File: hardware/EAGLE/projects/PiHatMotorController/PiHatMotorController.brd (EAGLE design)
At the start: 100 x 80 mm, 86 parts, among them IC2_0_PC JP, U0-C1 0.1uF, U0-C2 1nF, U0-C3 0.22uF, U0-C4 0.1uF, U0-C5 0.22uF, U0-R1 4.7k, U0-R2 47k, U0-R3 10k, U0-R4 10k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

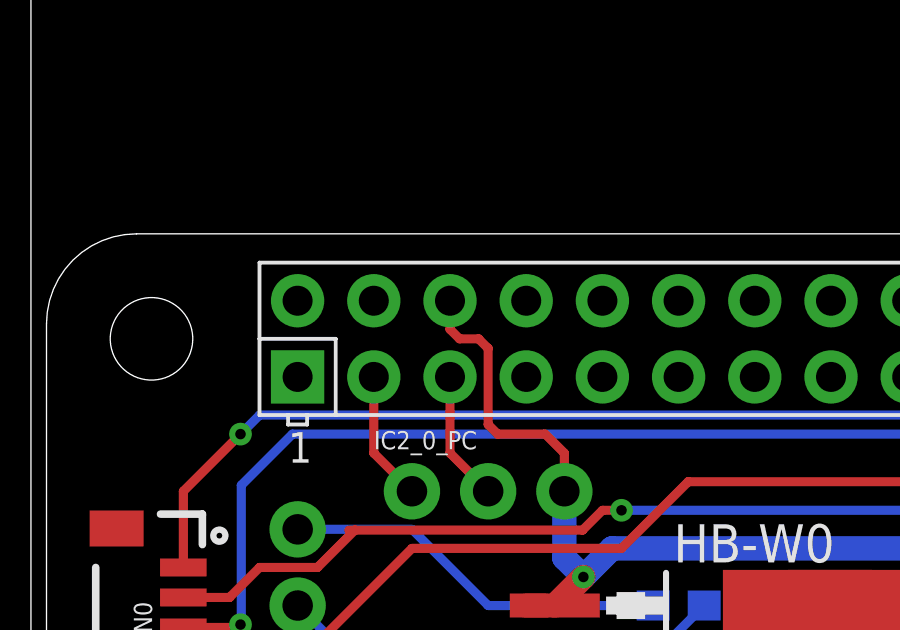
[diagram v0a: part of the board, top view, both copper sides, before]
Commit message: teensy32 board added
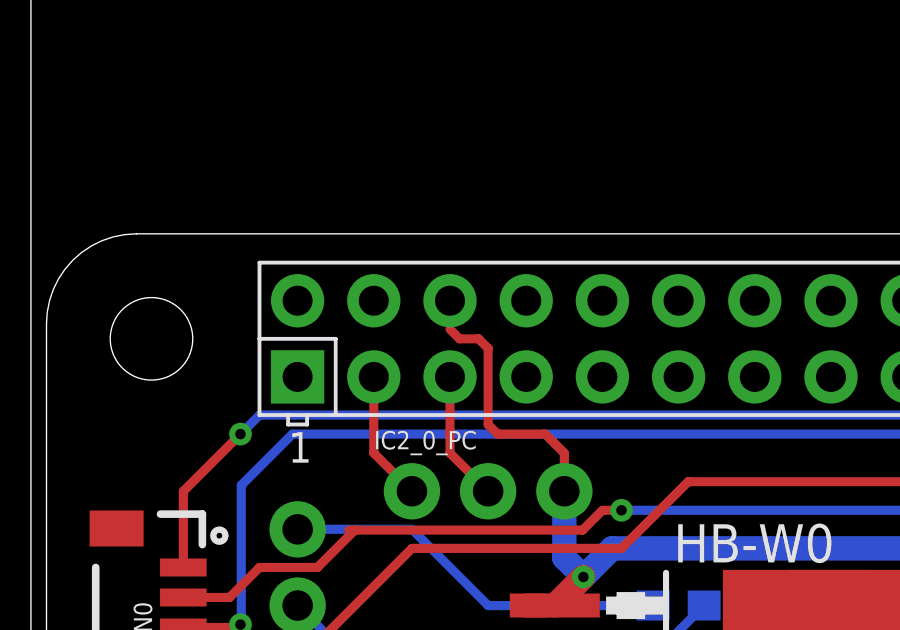
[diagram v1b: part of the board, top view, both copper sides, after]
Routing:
- net GND: track 401.0 -> 400.1 mm
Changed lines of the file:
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@@
 </signal>
 <signal name="GND">
-<contactref element="X1" pad="6"/>
 <contactref element="HB-W0" pad="1" route="any" routetag="G$1.GND"/>
 <contactref element="W0-C3" pad="1"/>
@@
 <wire x1="15.24" y1="53.0225" x2="14.9225" y2="53.34" width="0.3048" layer="1"/>
 <wire x1="14.9225" y1="53.34" x2="14.2875" y2="53.34" width="0.3048" layer="1"/>
-<wire x1="13.968159375" y1="53.659340625" x2="13.968159375" y2="54.61074375" width="0.3048" layer="1"/>
 <wire x1="14.2875" y1="53.34" x2="13.968159375" y2="53.659340625" width="0.3048" layer="1"/>
 <contactref element="BATTERY" pad="3"/>
@@
 <wire x1="57.785" y1="9.525" x2="57.15" y2="8.89" width="0.8128" layer="16"/>
 <wire x1="57.15" y1="8.89" x2="57.15" y2="5.08" width="0.8128" layer="16"/>
+<contactref element="X1" pad="6"/>
 <wire x1="39.155" y1="36.83" x2="39.155" y2="39.37" width="0" layer="19" extent="16-16"/>
 <wire x1="17.145" y1="44.45" x2="17.4625" y2="44.45" width="0" layer="19" extent="1-1"/>
+<wire x1="13.968159375" y1="54.61074375" x2="13.968159375" y2="53.659340625" width="0" layer="19" extent="1-1"/>
 <wire x1="34.71" y1="39.37" x2="34.71" y2="41.91" width="0" layer="19" extent="16-16"/>
 <wire x1="39.155" y1="27.94" x2="39.155" y2="25.4" width="0" layer="19" extent="16-16"/>

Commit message: PiHatMotorController checked
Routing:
- net GND: track 400.1 -> 415.6 mm
- net VI: track 272.6 -> 275.4 mm
- net 3.3V: track 175.3 -> 177.8 mm
- net U0: track 52.4 -> 50.6 mm
